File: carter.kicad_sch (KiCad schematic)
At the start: 14 parts, among them J1 USB C, J2 Micro_SD_Card, U1 CH340C

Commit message: near v1
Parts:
- added C2: 0.1uF, Capacitor_SMD:C_0603_1608Metric, symbol Device:C
- C1: LCSC (none) -> C14663
- J1: LCSC (none) -> C2988369
- J2: LCSC (none) -> C393941
- R1, R2: LCSC (none) -> C23186
- R3, R4, R5, R6, R7: footprint Resistor_SMD:R_0603_1608Metric -> Resistor_SMD:R_0805_2012Metric; LCSC (none) -> C2828840
- R8: value R -> 220; LCSC (none) -> C4190
- U1: LCSC (none) -> C7464026
- U2: footprint LeapFrog:LeapFrog-Cart -> LeapFrog:Cartridge
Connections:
- net +3V3: now also C2.1
- net GND: now also C2.2
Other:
- moved on the sheet: C1

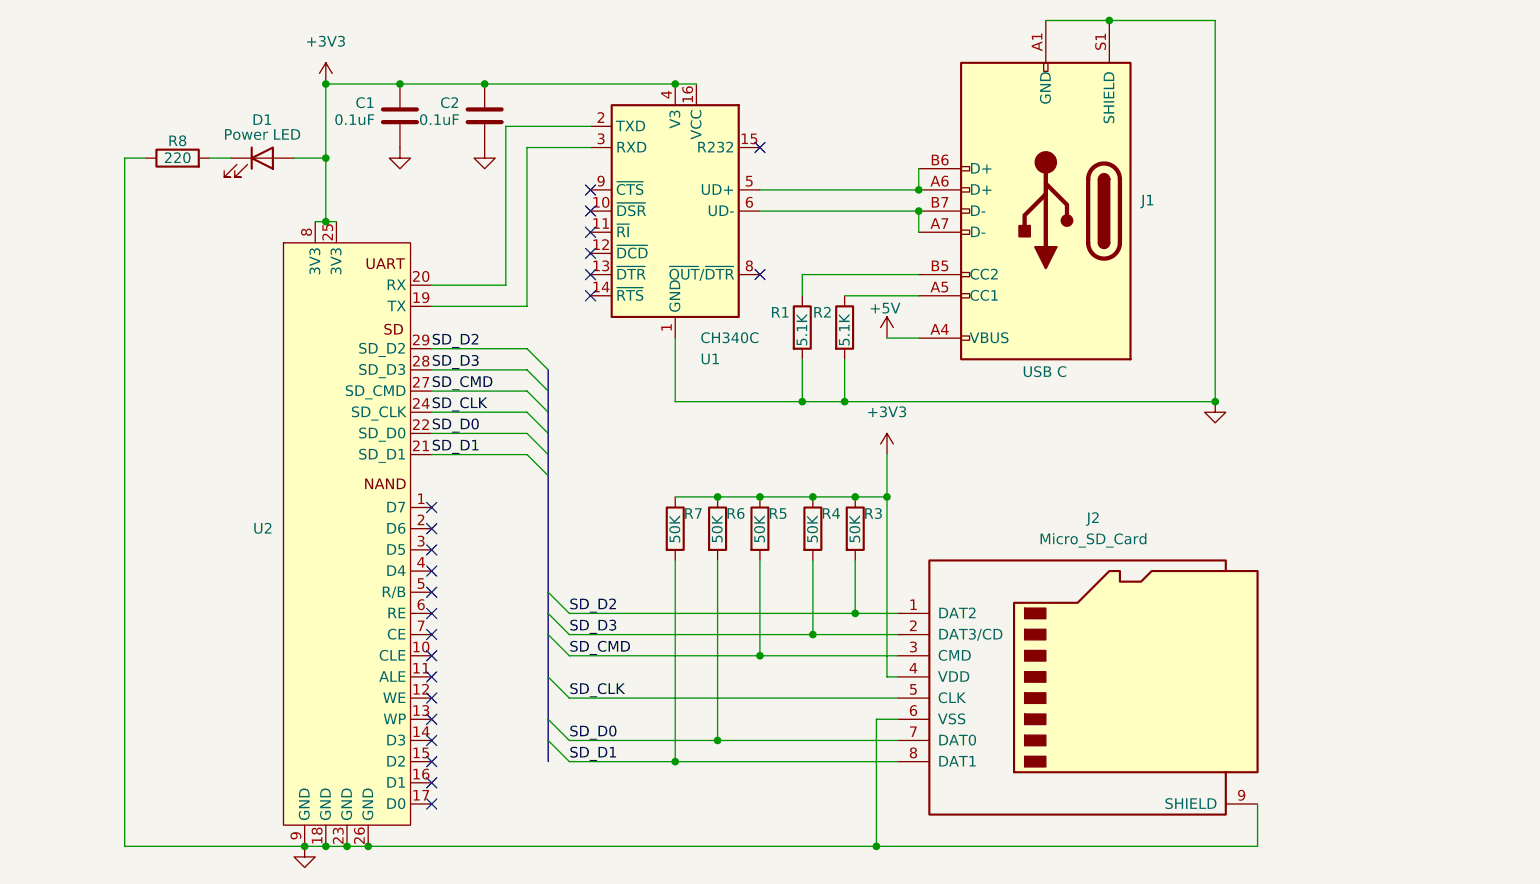
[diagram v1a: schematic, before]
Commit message: fix: usb-c connectivity
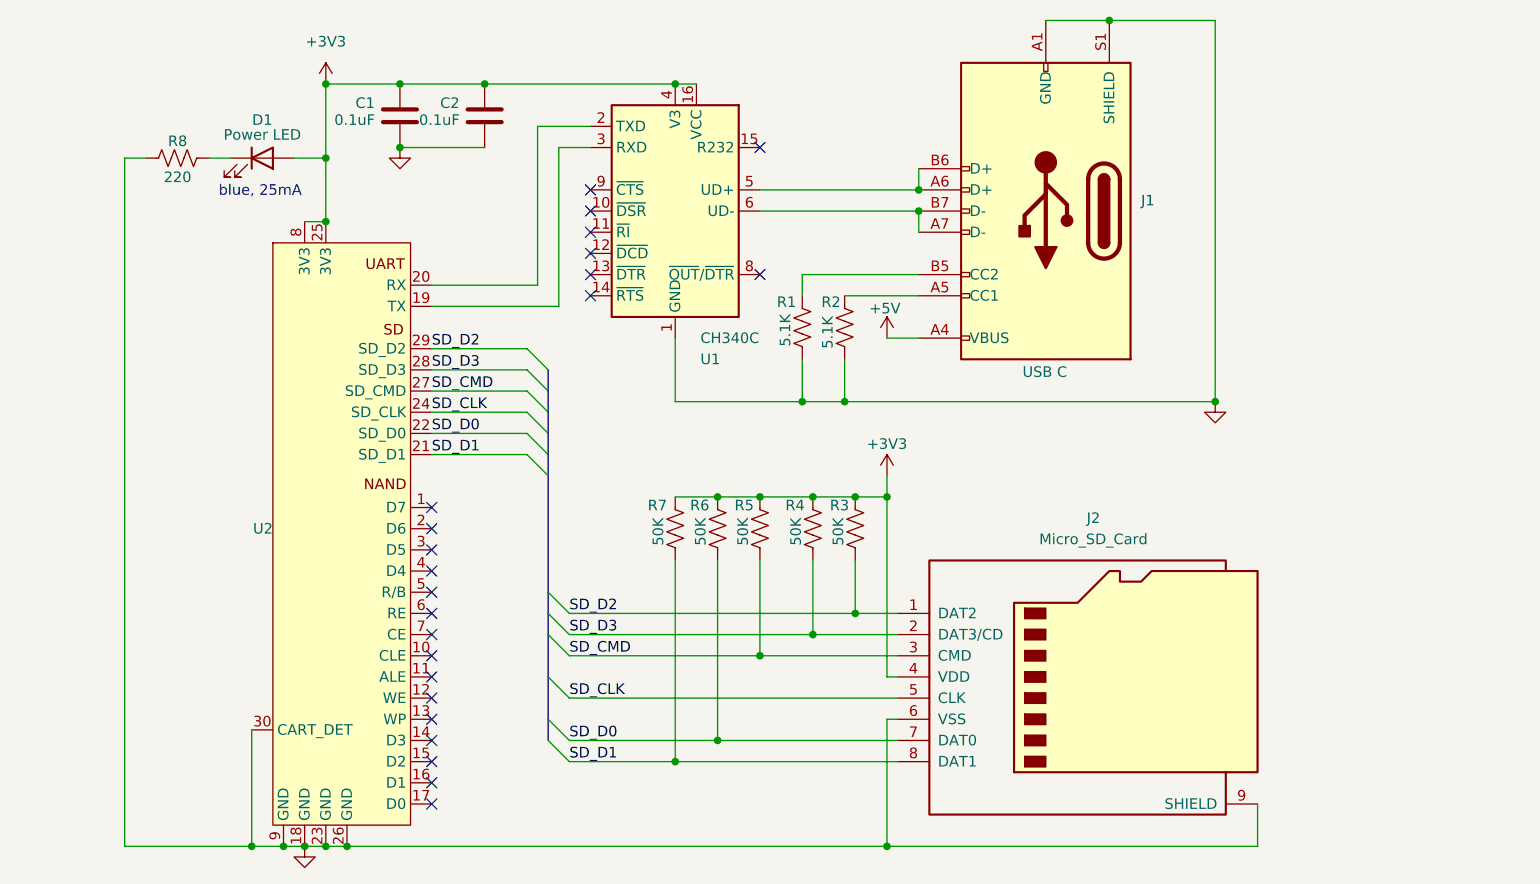
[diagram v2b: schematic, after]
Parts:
- D1: LCSC (none) -> C965807
- R1, R2, R3, R4, R5, R6, R7, R8: symbol Device:R -> Device:R_US
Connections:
- net GND: now also U2.30 (CART_DET)
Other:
- note added: "blue, 25mA"

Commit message: redesign with ams1117-3.3
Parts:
- added C3: 22uF, Capacitor_SMD:C_0603_1608Metric, symbol Device:C
- added C4: 0.1uF, Capacitor_SMD:C_0603_1608Metric, symbol Device:C
- added U3: AMS1117-3.3, Package_TO_SOT_SMD:SOT-223-3_TabPin2, symbol Regulator_Linear:AMS1117-3.3
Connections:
- net +3V3: now also C3.1, U3.2 (VO)
- net +5V: now also C4.1, U3.3 (VI)
- net GND: now also C3.2, C4.2, U3.1 (GND)
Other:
- company: (none) -> kiboigo.com
- moved on the sheet: C1, C2, D1, J1, J2, R1, R2, R3, R4, R5, R6, R7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
